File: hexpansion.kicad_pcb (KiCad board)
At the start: 2 copper layers, 32 x 36.6 mm, 44 parts, among them J1 Hexpansion-Connector, J2 Conn_ARM_SWD_TagConnect_TC2030, Q1 2N7002, Q2 2N7002, Q3 2N7002, Q4 2N7002

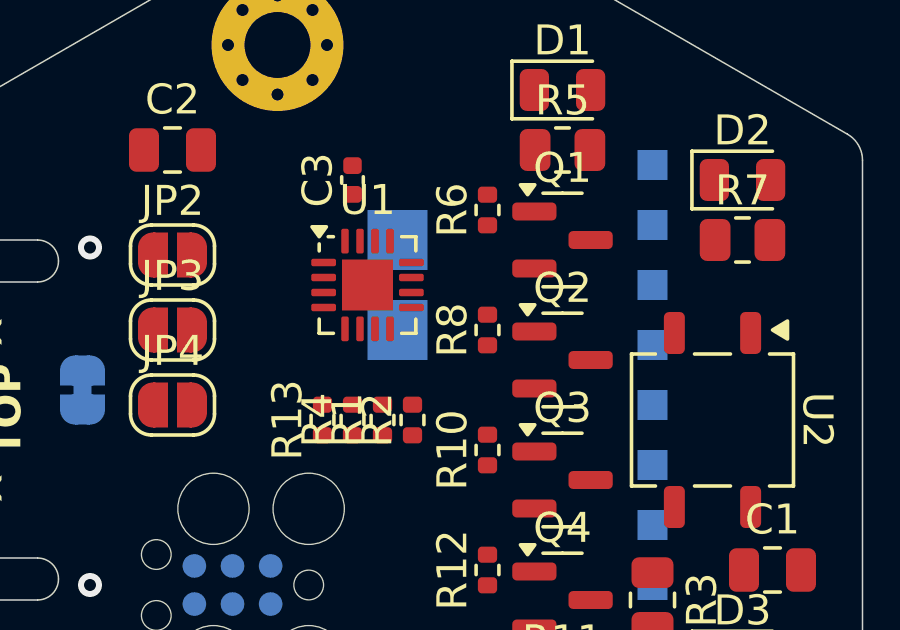
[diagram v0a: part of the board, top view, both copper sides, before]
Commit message: setup board, rough place
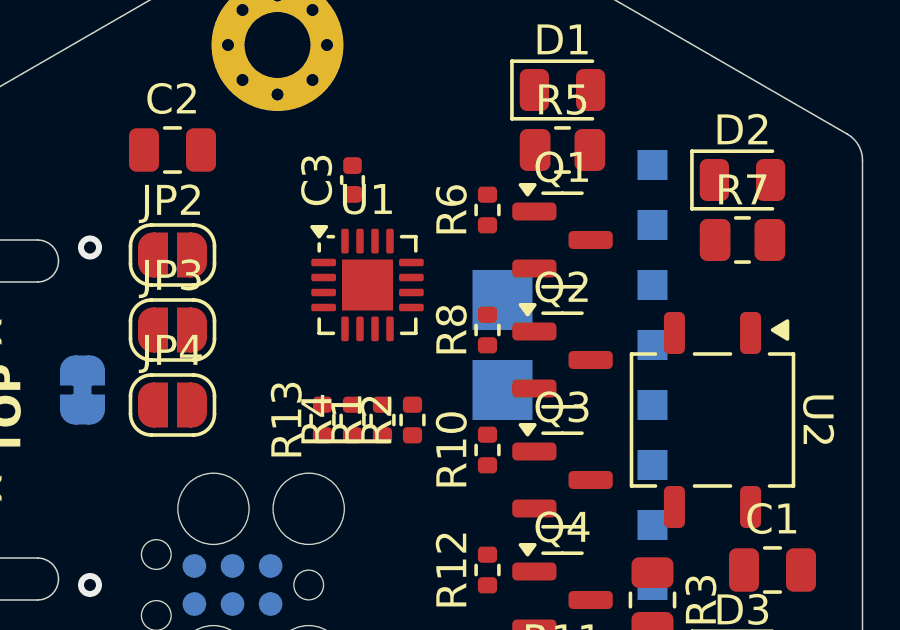
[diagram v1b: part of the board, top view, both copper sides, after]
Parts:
- moved TP1 4.03 mm to (120.0, 96.0)
- moved TP2 4.03 mm to (120.0, 99.0)
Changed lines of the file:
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@@
 	(footprint "TestPoint:TestPoint_Pad_2.0x2.0mm"
 		(layer "B.Cu")
-		(at 116.5 97 180)
+		(at 120 99 180)
 		(descr "SMD rectangular pad as test Point, square 2.0mm side length")
 		(tags "test point SMD pad rectangle square")
@@
 	(footprint "TestPoint:TestPoint_Pad_2.0x2.0mm"
 		(layer "B.Cu")
-		(at 116.5 94 180)
+		(at 120 96 180)
 		(descr "SMD rectangular pad as test Point, square 2.0mm side length")
 		(tags "test point SMD pad rectangle square")

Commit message: routing tweaks
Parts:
- moved TP3 10.0 mm to (125.0, 105.5)
- moved TP10 8.00 mm to (125.0, 93.5)
- moved TP8 8.00 mm to (125.0, 91.5)
- moved C2 7.50 mm to (116.5, 91.0), turned to 90 degrees
- moved TP6 6.00 mm to (125.0, 99.5)
- moved TP9 6.00 mm to (125.0, 97.5)
- moved TP5 4.00 mm to (125.0, 101.5)
- moved TP7 4.00 mm to (125.0, 95.5)
- moved TP4 2.00 mm to (125.0, 103.5)
- moved C3 0.50 mm to (115.0, 91.5)
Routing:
- net +3.3V: track 0.80 -> 102.0 mm, vias 0 -> 1
- net GND: track 0.00 -> 37.5 mm, vias 2 -> 25
- net /~{RST}: track 0.00 -> 28.6 mm, vias 0 -> 1
- net /SCL: track 0.00 -> 24.8 mm, vias 0 -> 1
- net /SDA: track 0.00 -> 24.0 mm, vias 0 -> 1
- net /IR_RX: track 0.00 -> 20.9 mm, vias 0 -> 2
- net Net-(U1-PA12): track 0.00 -> 19.3 mm, vias 0 -> 1
- net Net-(U1-PB1): track 0.00 -> 17.5 mm, vias 0 -> 1
- net /SWDIO: track 0.00 -> 17.4 mm, vias 0 -> 1
- net /IR_TX: track 0.00 -> 17.3 mm
- net /HS_H: track 0.00 -> 17.2 mm, vias 0 -> 2
- net Net-(U1-PA8): track 0.00 -> 15.8 mm, vias 0 -> 1
- net Net-(U1-PA4): track 0.00 -> 15.4 mm, vias 0 -> 1
- net /SWCLK: track 0.00 -> 14.6 mm, vias 0 -> 3
- net Net-(U1-PA1): track 0.00 -> 14.4 mm, vias 0 -> 1
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
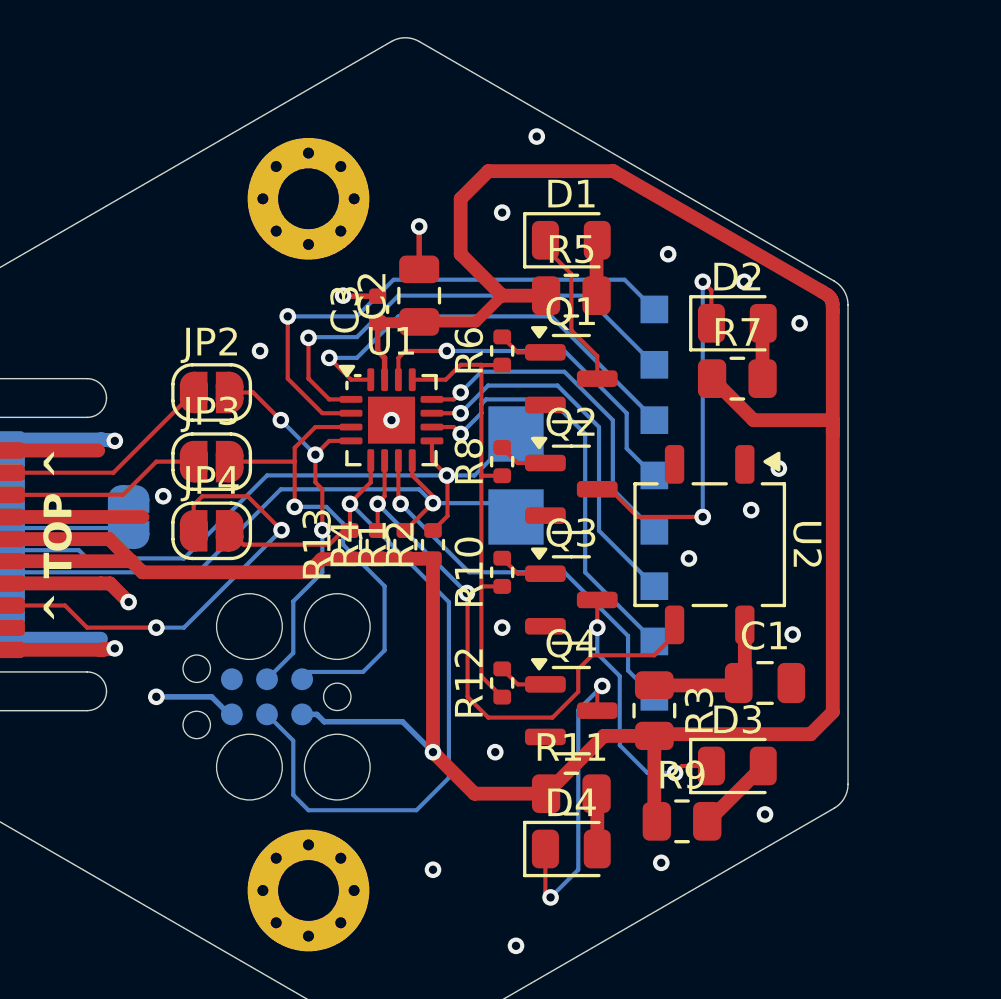
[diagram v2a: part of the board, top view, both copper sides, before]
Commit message: clean up silk/fab
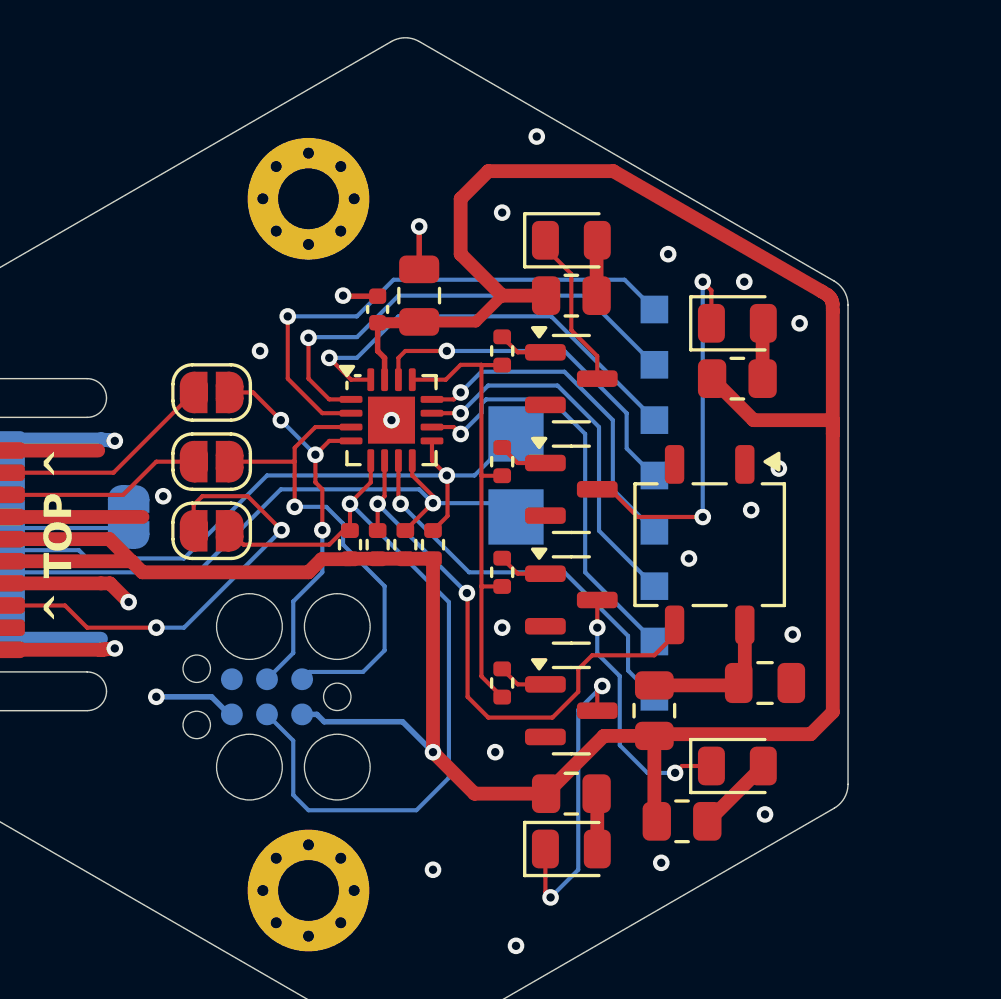
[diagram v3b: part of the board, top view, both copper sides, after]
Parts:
- JP2: value SolderJumper_2_Open -> SWCLK
- JP3: value SolderJumper_2_Open -> SWDIO
- JP4: value SolderJumper_2_Open -> ~{RST}
- TP1: value TestPoint -> SCL
- TP10: value TestPoint_Small -> PB1
- TP2: value TestPoint -> SDA
- TP3: value TestPoint_Small -> PA1
- TP4: value TestPoint_Small -> PA4
- TP5: value TestPoint_Small -> PA5
- TP6: value TestPoint_Small -> PA6
- TP7: value TestPoint_Small -> PA8
- TP8: value TestPoint_Small -> PA12
- TP9: value TestPoint_Small -> PB0
- U1: value ~ -> PY32F002AW15U
- U2: value ~ -> IRM-H638T/TR2
